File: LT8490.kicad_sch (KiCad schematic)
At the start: 88 parts

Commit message: cleaned up routing
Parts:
- added J1, J10, J2, J3, J4, J5, J7, J8, J9: Conn_01x01, custom-footprints:castellated_05mm, symbol Connector_Generic:Conn_01x01
- added J6: (no value), symbol Connector_Generic:Conn_01x01
- added NT6, NT7: NetTie_2, NetTie:NetTie-2_SMD_Pad0.5mm, symbol Device:NetTie_2
- added R1: 10, Resistor_SMD:R_0603_1608Metric, symbol Device:R_US
- C15, C20, C37, C40: value (none) -> 100nF; footprint (none) -> Capacitor_SMD:C_0603_1608Metric
- C16: value (none) -> 33uF; footprint (none) -> Capacitor_Tantalum_SMD:CP_EIA-7343-30_AVX-N
- C17: value (none) -> 2.2uF; footprint (none) -> Capacitor_SMD:C_0603_1608Metric
- C18, C22, C25: value (none) -> 2.2uF; footprint (none) -> Capacitor_SMD:C_0805_2012Metric
- C19, C34, C39: value (none) -> 1uF; footprint (none) -> Capacitor_SMD:C_0603_1608Metric
- C21, C24, C38: value (none) -> 4.7uF; footprint (none) -> Capacitor_SMD:C_0603_1608Metric
- C23: value (none) -> 10nF; footprint (none) -> Capacitor_SMD:C_0603_1608Metric
- C26, C35: value (none) -> 470nF; footprint (none) -> Capacitor_SMD:C_0603_1608Metric
- C27: value (none) -> 220pF; footprint (none) -> Capacitor_SMD:C_0603_1608Metric
- C28: value (none) -> 6.8nF; footprint (none) -> Capacitor_SMD:C_0603_1608Metric
- C29, C33: value (none) -> 220nF; footprint (none) -> Capacitor_SMD:C_0603_1608Metric
- C30: value (none) -> 68nF; footprint (none) -> Capacitor_SMD:C_0603_1608Metric
- C31, C32: value (none) -> 3.3nF; footprint (none) -> Capacitor_SMD:C_0603_1608Metric
- C36, C41: value (none) -> 10uF; footprint (none) -> Capacitor_SMD:C_0805_2012Metric
- C42: value (none) -> 47uF; footprint (none) -> Capacitor_Tantalum_SMD:CP_EIA-7343-30_AVX-N
- C43: value (none) -> 1nF; footprint (none) -> Capacitor_SMD:C_0603_1608Metric
- D1, D2: value (none) -> MBR1020VL; footprint (none) -> Diode_SMD:D_SOD-123F
- D12, D13: value (none) -> CMMR1U-02 TR; footprint (none) -> Diode_SMD:D_SOD-123F
- L3: value (none) -> 3.3uH; footprint (none) -> custom-footprints:L_SRP1770C
- NT1: value (none) -> NetTie_2; footprint (none) -> NetTie:NetTie-2_SMD_Pad0.5mm
- Q1, Q2, Q3, Q4: value (none) -> Si7106DN; footprint (none) -> custom-footprints:SIS862DNT1GE3
- Q5: value (none) -> BSS84; footprint (none) -> custom-footprints:BSS138DWQ-7
- Q6: value (none) -> MBT2222ADW1T1; footprint (none) -> Package_TO_SOT_SMD:SOT-363_SC-70-6
- R17: value (none) -> 86.6K; footprint (none) -> Resistor_SMD:R_0603_1608Metric
- R18: value (none) -> 16.5K; footprint (none) -> Resistor_SMD:R_0603_1608Metric
- R19, R26: value (none) -> 124K; footprint (none) -> Resistor_SMD:R_0603_1608Metric
- R20: value (none) -> 196K; footprint (none) -> Resistor_SMD:R_0603_1608Metric
- R21: value (none) -> 8.06K; footprint (none) -> Resistor_SMD:R_0603_1608Metric
- R22, R30: value (none) -> 21K; footprint (none) -> Resistor_SMD:R_0603_1608Metric
- R23: value (none) -> 110K; footprint (none) -> Resistor_SMD:R_0603_1608Metric
- R24: value (none) -> 35.7K; footprint (none) -> Resistor_SMD:R_0603_1608Metric
- R25: value (none) -> 30.1K; footprint (none) -> Resistor_SMD:R_0603_1608Metric
- R27: value (none) -> 0.025; footprint (none) -> Resistor_SMD:R_1206_3216Metric
- R28: value (none) -> 105K; footprint (none) -> Resistor_SMD:R_0603_1608Metric
- R29, R35, R42, R44, R50: value (none) -> 0; footprint (none) -> Resistor_SMD:R_0603_1608Metric
- R31: value (none) -> 3.01K; footprint (none) -> Resistor_SMD:R_0603_1608Metric
- R32, R39: value (none) -> 2; footprint (none) -> Resistor_SMD:R_0603_1608Metric
- R33: value (none) -> 4.99K; footprint (none) -> Resistor_SMD:R_0603_1608Metric
- R34: value (none) -> 53.6K; footprint (none) -> Resistor_SMD:R_0603_1608Metric
- R36, R37, R48, R55: value (none) -> 10; footprint (none) -> Resistor_SMD:R_0603_1608Metric
- R38: value (none) -> 0.001; footprint (none) -> Resistor_SMD:R_1206_3216Metric
- R40, R54: value (none) -> 200K; footprint (none) -> Resistor_SMD:R_0603_1608Metric
- R41: value (none) -> 1; footprint (none) -> Resistor_SMD:R_0603_1608Metric
- R43: value (none) -> 23.2K; footprint (none) -> Resistor_SMD:R_0603_1608Metric
- R45: value (none) -> 11.5K; footprint (none) -> Resistor_SMD:R_0603_1608Metric
- R46: value (none) -> 0.05; footprint (none) -> Resistor_SMD:R_1206_3216Metric
- R47: value (none) -> 10K; footprint (none) -> Resistor_SMD:R_0603_1608Metric
- R49: value (none) -> 121K; footprint (none) -> Resistor_SMD:R_0603_1608Metric
- R51: value (none) -> 154K; footprint (none) -> Resistor_SMD:R_0603_1608Metric
- R52: value (none) -> 23.7K; footprint (none) -> Resistor_SMD:R_0603_1608Metric
- R53, R56, R57, R58: value (none) -> ???; footprint (none) -> Resistor_SMD:R_0603_1608Metric
- U4: value (none) -> LT8490EUKJPBF; footprint (none) -> custom-footprints:LT8490EUKJ#PBF
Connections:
- net CSNIN: now also R1.1; no longer C26.2, U4.44 (CSNIN)
- net GND: now also R38.2, J1.1 (Pin_1), J2.1 (Pin_1), J5.1 (Pin_1), J6.1 (Pin_1)
- net REG_{FAULT}: now also J10.1 (Pin_1)
- net REG_{STATUS}: now also J9.1 (Pin_1)
- net VBATT: now also J7.1 (Pin_1), J8.1 (Pin_1), NT7.2; no longer Q5.1 (S2), R50.1, R57.2
- net VSOLAR: now also J3.1 (Pin_1), J4.1 (Pin_1), NT6.2; no longer C17.1, R17.1, R20.1, R23.1, U4.46 (VIN)
- net at C32.2, C43.2, U4.12 (CSN): now also R37.1; no longer R37.2
- net FBOUT_0: now reaches Q5.6 (D1), R50.2, R51.1
- net BG2_: now reaches R39.2, U4.25 (BG2)
- new net: NT1.2, R37.2
- new net CSNIN_0: C26.2, R1.2, U4.44 (CSNIN)
- new net FBIN: C17.1, NT6.1, R17.1, R20.1, R23.1, U4.46 (VIN)
- new net FBOUT: NT7.1, Q5.1 (S2), R50.1, R57.2
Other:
- moved on the sheet: R37, R39

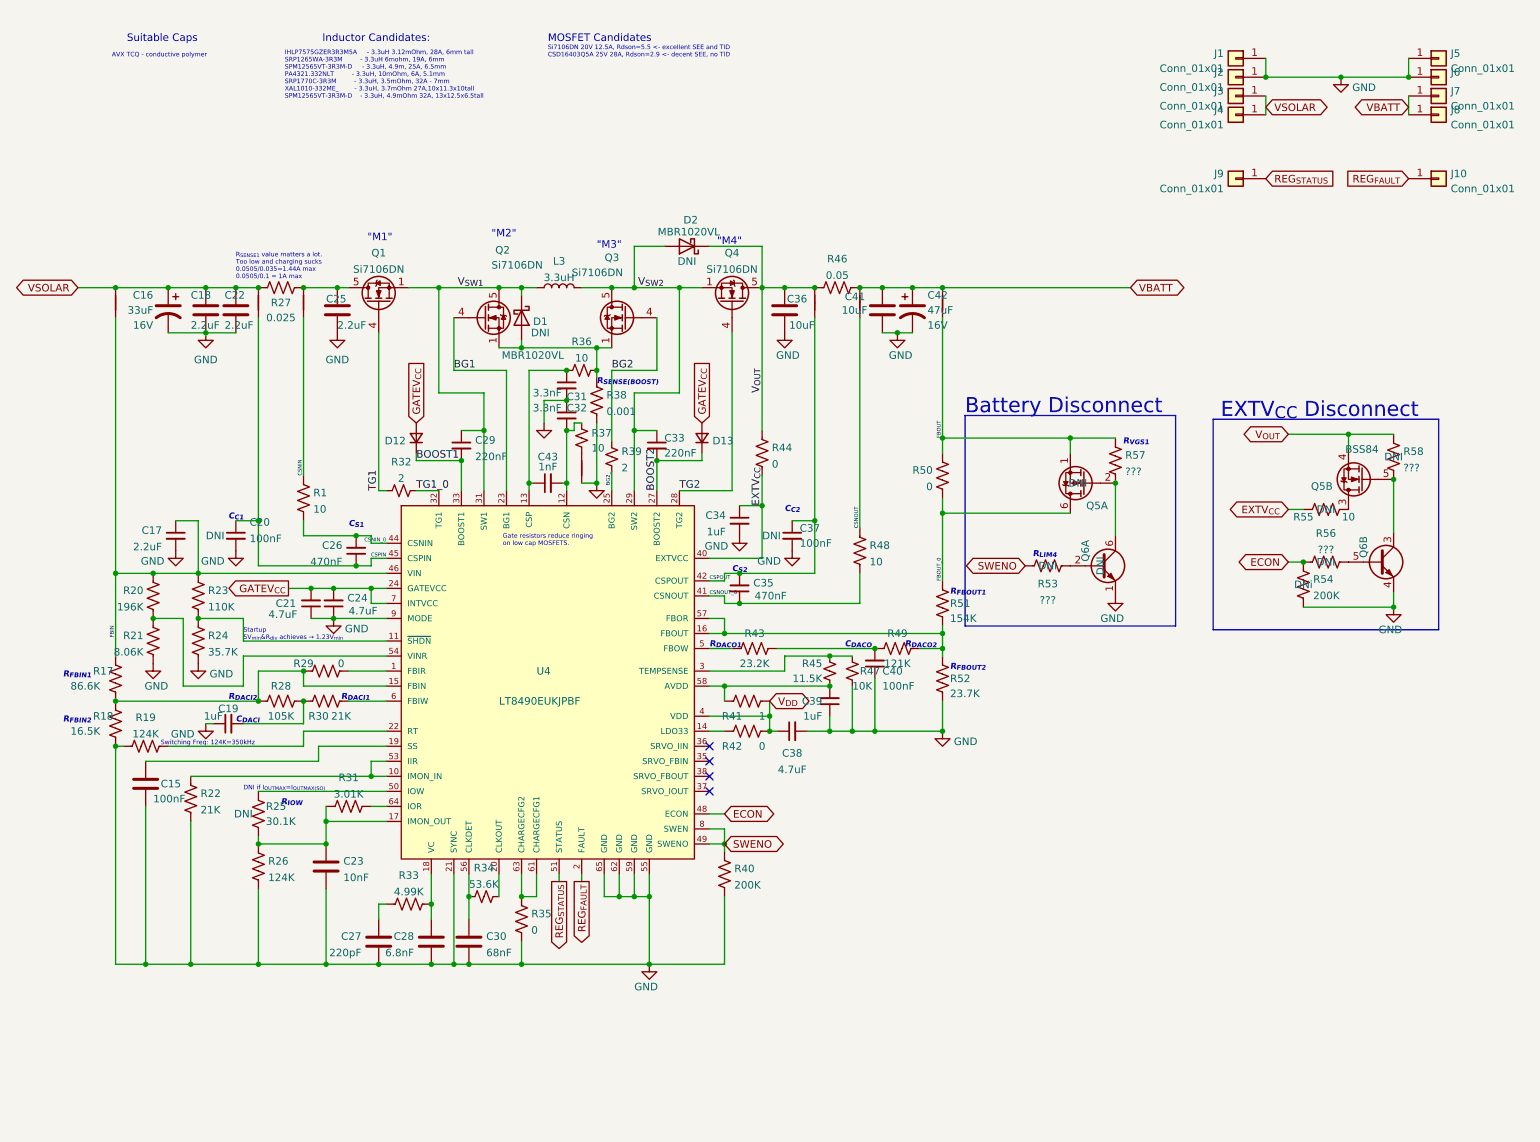
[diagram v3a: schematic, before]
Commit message: passed DRC & extra SS labeling
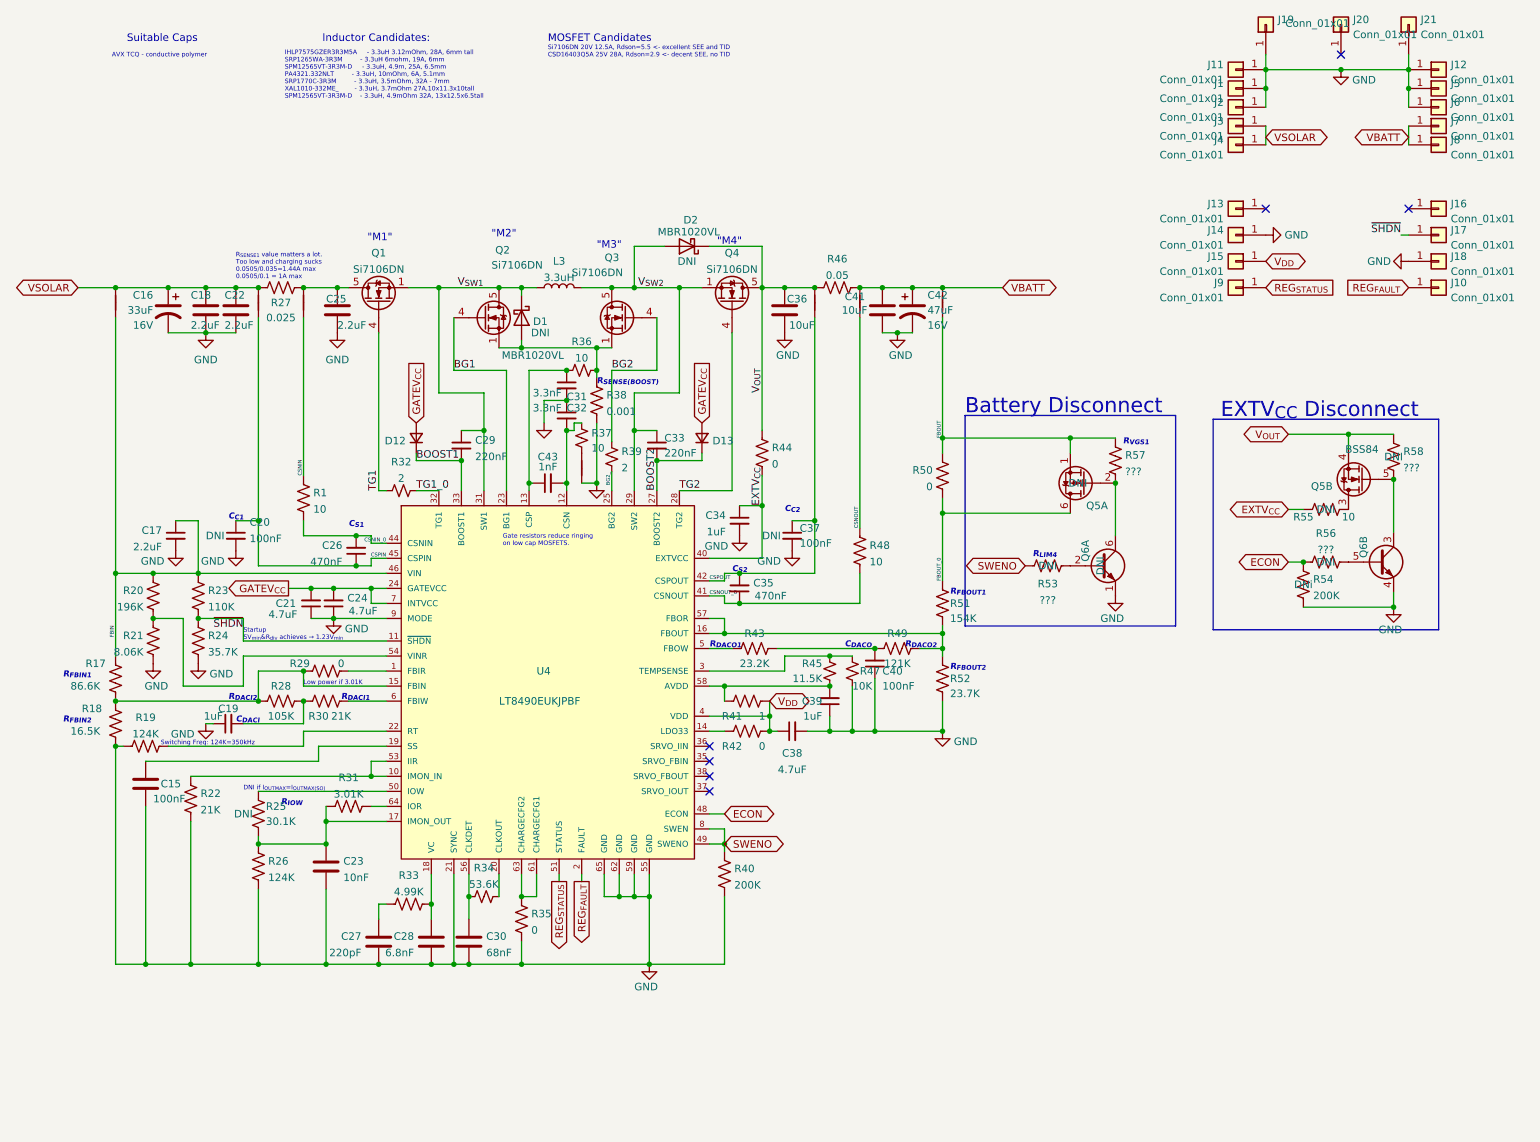
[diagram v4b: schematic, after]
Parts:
- added J11, J12, J13, J14, J15, J16, J17, J18, J19, J20, J21: Conn_01x01, custom-footprints:castellated_05mm, symbol Connector_Generic:Conn_01x01
- J6: value (none) -> Conn_01x01; footprint (none) -> custom-footprints:castellated_05mm
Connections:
- net GND: now also J11.1 (Pin_1), J12.1 (Pin_1), J14.1 (Pin_1), J18.1 (Pin_1), J19.1 (Pin_1), J21.1 (Pin_1)
- net V_{DD}: now also J15.1 (Pin_1)
- net ~{SHDN}: now reaches R23.2, R24.1, U4.11 (~{SHDN})
- net ~{SHDN}: now also J17.1 (Pin_1)
- no-connect marks 4 -> 7
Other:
- note added: "Low power if 3.01K"
- moved on the sheet: J1, J10, J2, J3, J4, J5, J6, J7, J8, J9

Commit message: Added LT8491 functionality (I2C)
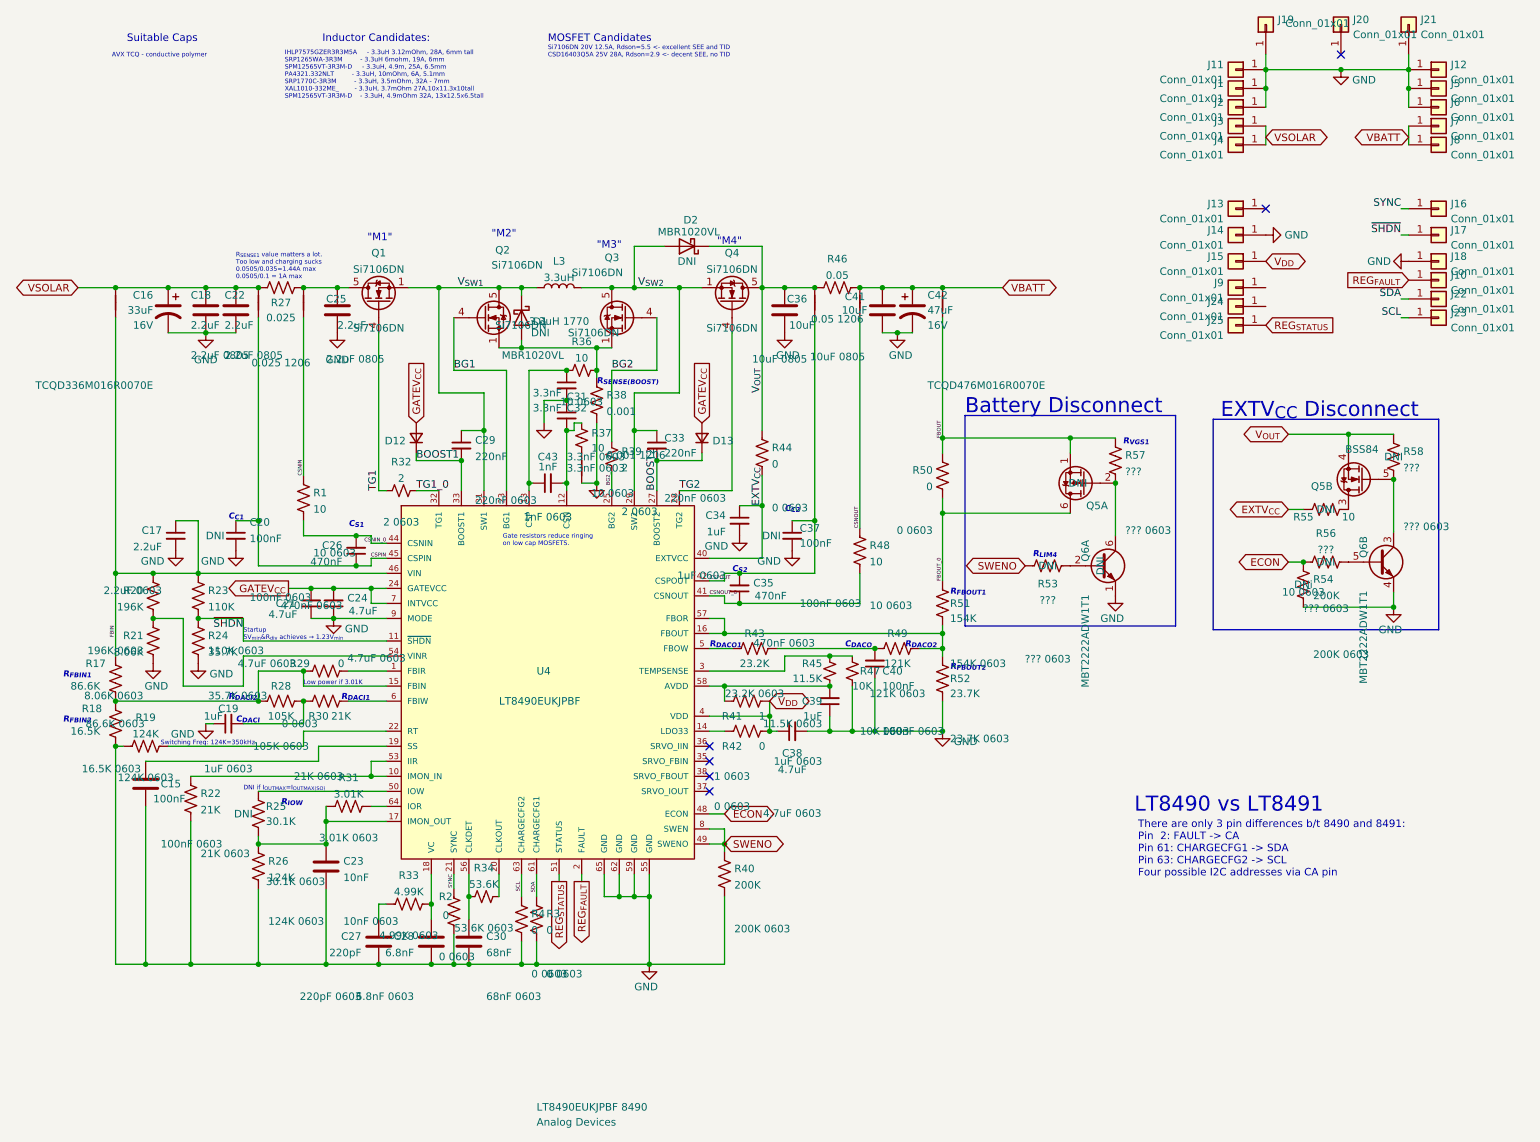
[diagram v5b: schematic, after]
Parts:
- removed R35: 0, Resistor_SMD:R_0603_1608Metric, symbol Device:R_US
- added J22, J23, J24, J25: Conn_01x01, custom-footprints:castellated_05mm, symbol Connector_Generic:Conn_01x01
- added R2, R3, R4: 0, Resistor_SMD:R_0603_1608Metric, symbol Device:R_US
- C16: Manufacturer_Part_Number (none) -> TCQD336M016R0070E; PN TCQD336M016R0070E -> (none)
- C42: Manufacturer_Part_Number (none) -> TCQD476M016R0070E; PN TCQD476M016R0070E -> (none)
- NT1, NT2, NT3, NT4, NT5, NT6, NT7: DNI (none) -> DNI
- Q1, Q2, Q3, Q4: Manufacturer_Part_Number (none) -> Si7106DN
- Q5: Height 1.1 -> (none); Manufacturer_Part_Number BSS138DWQ-7 -> (none); Mouser Part Number 621-BSS138DWQ-7 -> (none); Mouser Price/Stock https://www.mouser.co.uk/ProductDetail/Diodes-Incorporated/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 -> (none)
- Q6: Manufacturer_Part_Number (none) -> MBT2222ADW1T1
- U4: Manufacturer_Name (none) -> Analog Devices; automotive No -> (none); category IC -> (none); device class L1 Integrated Circuits (ICs) -> (none); device class L2 Power Management ICs -> (none); device class L3 Battery Management -> (none); digikey description IC BATT CHG MULTI-CHEM 64QFN -> (none); digikey part number LT8490EUKJ#PBF-ND -> (none); footprint url https://www.analog.com/media/en/package-pcb-resources/packa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 -> (none); height 0.8mm -> (none); lead free Yes -> (none); library id 22bf639927d060ab -> (none); manufacturer Analog Devices -> (none); max junction temp +125°C -> (none); max supply voltage 80V -> (none); min supply voltage 6V -> (none); mouser description Switching Battery Charger Controller Lead-Acid/Li-Ion 1.3V 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 -> (none); mouser part number 584-LT8490EUKJ#PBF -> (none); nominal supply current 2.65-4mA -> (none); number of cells 1 -> (none); number of outputs 1 -> (none); package QFN64 -> (none); rohs Yes -> (none); standoff height 0mm -> (none); temperature range high +125°C -> (none); temperature range low -40°C -> (none)
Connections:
- net GND: now also R2.2, R3.2, R4.2; no longer U4.21 (SYNC)
- net REG_{STATUS}: now also J25.1 (Pin_1); no longer J9.1 (Pin_1)
- net SCL: now reaches U4.63 (CHARGECFG2)
- net SCL: now also J23.1 (Pin_1), R4.1; no longer U4.61 (CHARGECFG1)
- net SYNC: now reaches J16.1 (Pin_1)
- net SYNC: now also U4.21 (SYNC), R2.1
- new net SDA: J22.1 (Pin_1), R3.1, U4.61 (CHARGECFG1)
- no-connect marks 7 -> 6
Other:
- note added: "IHLP7575GZER3R3M5A t- 3.3uH 3.12mOhm, 28A, 6mm tall SRP1265WA-3R3M tt- 3.3uH 6mohm, 19A, 6mm SPM12565VT-3R3M-D t- 3.3uH, 4.9m, 25A, 6.5mm PA4321.332NLT tt- 3.3uH, 10mOhm, 6A, 5.1mm SRP1770C-3R3M tt- 3.3uH, 3.5mOhm, 32A - 7mm XAL1010-332ME_tt- 3.3uH, 3.7mOhm 27A,10x11.3x10tall SPM12565VT-3R3M-Dt- 3.3uH, 4.9mOhm 32A, 13x12.5x6.5tall"
- note added: "LT8490 vs LT8491"
- note added: "There are only 3 pin differences b/t 8490 and 8491: Pin 2: FAULT -> CA Pin 61: CHARGECFG1 -> SDA Pin 63: CHARGECFG2 -> SCL Four possible I2C addresses via CA pin"
- note removed: "IHLP7575GZER3R3M5A - 3.3uH 3.12mOhm, 28A, 6mm tall SRP1265WA-3R3M - 3.3uH 6mohm, 19A, 6mm SPM12565VT-3R3M-D - 3.3uH, 4.9m, 25A, 6.5mm PA4321.332NLT - 3.3uH, 10mOhm, 6A, 5.1mm SRP1770C-3R3M - 3.3uH, 3.5mOhm, 32A - 7mm XAL1010-332ME_ - 3.3uH, 3.7mOhm 27A,10x11.3x10tall SPM12565VT-3R3M-D - 3.3uH, 4.9mOhm 32A, 13x12.5x6.5tall"
- moved on the sheet: J10
